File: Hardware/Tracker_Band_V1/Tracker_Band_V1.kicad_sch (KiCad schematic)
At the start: 5 parts, among them J1 USB_C_USB20, U1 ESP32-C3-MINI-1-N4, U2 BNO085

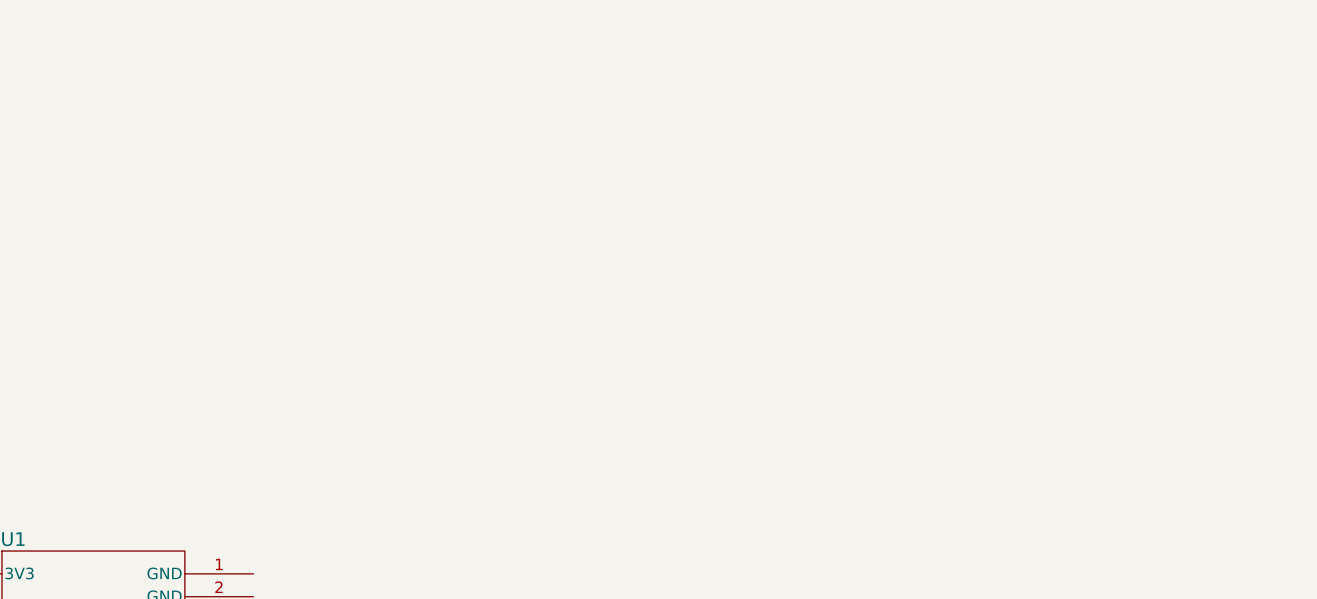
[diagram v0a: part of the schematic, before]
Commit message: added custom power sym/fp
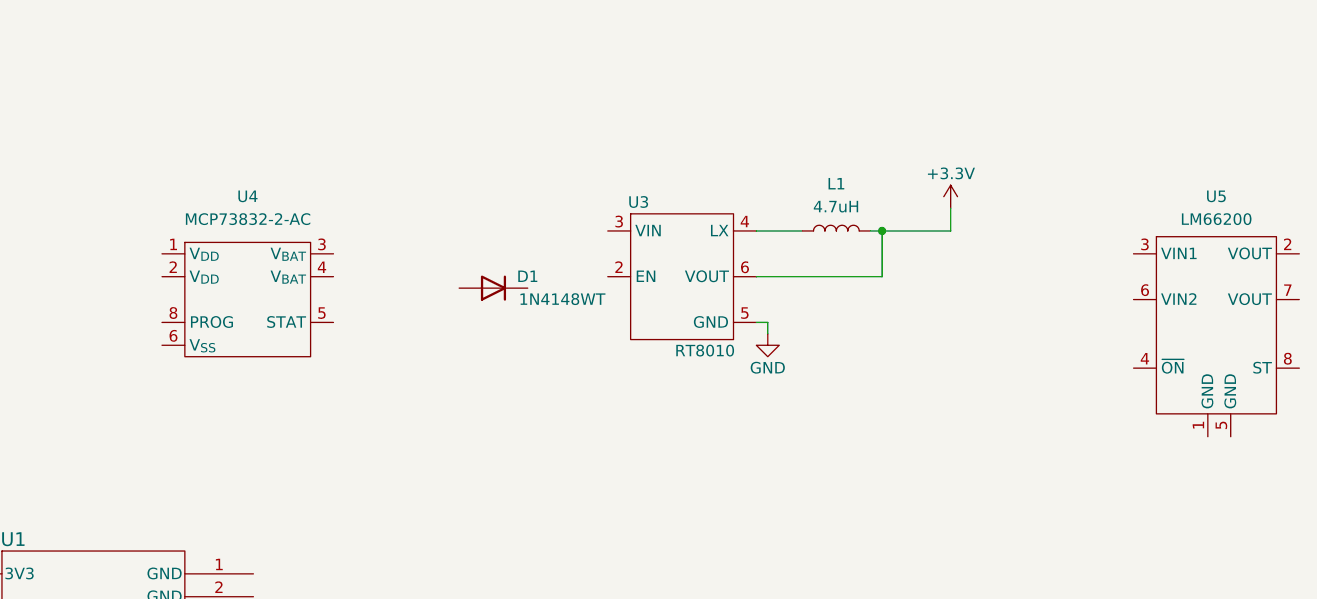
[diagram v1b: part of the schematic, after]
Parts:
- added D1: 1N4148WT, Diode_SMD:D_SOD-523, symbol Diode:1N4148WT
- added L1: 4.7uH, Inductor_SMD:L_Taiyo-Yuden_NR-30xx, symbol Device:L
- added U3: RT8010, Package_DFN_QFN:DFN-6-1EP_2x2mm_P0.65mm_EP1x1.6mm, symbol 00_tracker_sym:RT8010
- added U4: MCP73832-2-AC, Package_DFN_QFN:DFN-8-1EP_3x2mm_P0.5mm_EP1.7x1.4mm, symbol 00_tracker_sym:MCP73832-2-AC
- added U5: LM66200, 00_tracker_fp:SOT-5X3_DRL_TEX-L, symbol 00_tracker_sym:LM66200
- J1: footprint Connector_USB:USB_C_Receptacle_G-Switch_GT-USB-7010ASV -> 00_tracker_fp:USB_C_Receptacle_G-Switch_GT-USB-7010ASV_local3d
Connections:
- net +3.3V: now also L1.2, U3.6 (VOUT)
- net GND: now also U3.5 (GND)
- new net: L1.1, U3.4 (LX)
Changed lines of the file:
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@@
 (kicad_sch (version 20230121) (generator eeschema)
   (paper "A3")
+  (junction (at 278.13 64.77) (diameter 0) (color 0 0 0 0)
+  )
   (wire (pts (xy 125.73 114.3) (xy 125.73 115.57))
     (stroke (width 0) (type default))
   )
+  (wire (pts (xy 278.13 64.77) (xy 276.86 64.77))
+    (stroke (width 0) (type default))
+  )
+  (wire (pts (xy 264.16 69.85) (xy 278.13 69.85))
+    (stroke (width 0) (type default))
+  )
+  (wire (pts (xy 265.43 76.2) (xy 265.43 74.93))
+    (stroke (width 0) (type default))
+  )
+  (wire (pts (xy 278.13 69.85) (xy 278.13 64.77))
+    (stroke (width 0) (type default))
+  )
+  (wire (pts (xy 265.43 74.93) (xy 264.16 74.93))
+    (stroke (width 0) (type default))
+  )
   (wire (pts (xy 125.73 93.98) (xy 125.73 95.25))
     (stroke (width 0) (type default))
   )
+  (wire (pts (xy 285.75 62.23) (xy 285.75 64.77))
+    (stroke (width 0) (type default))
+  )
+  (wire (pts (xy 285.75 64.77) (xy 278.13 64.77))
+    (stroke (width 0) (type default))
+  )
   (wire (pts (xy 125.73 100.33) (xy 125.73 109.22))
+    (stroke (width 0) (type default))
+  )
+  (wire (pts (xy 264.16 64.77) (xy 269.24 64.77))
     (stroke (width 0) (type default))
   )
@@
     (effects (font (size 1.27 1.27)) (justify left bottom))
   )
+  (symbol (lib_id "Diode:1N4148WT") (at 234.95 71.12 180) (unit 1)
+    (in_bom yes) (on_board yes) (dnp no)
+    (property "Reference" "D1" (at 238.76 69.85 0)
+      (effects (font (size 1.27 1.27)))
+    )
+    (property "Value" "1N4148WT" (at 242.57 72.39 0)
+      (effects (font (size 1.27 1.27)))
+    )
+    (property "Footprint" "Diode_SMD:D_SOD-523" (at 234.95 66.675 0)
+      (effects (font (size 1.27 1.27)) hide)
+    )
+    (property "Datasheet" "https://www.diodes.com/assets/Datasheets/ds30396.pdf" (at 234.95 71.12 0)
+      (effects (font (size 1.27 1.27)) hide)
+    )
+    (property "Sim.Device" "D" (at 234.95 71.12 0)
+      (effects (font (size 1.27 1.27)) hide)
+    )
+    (property "Sim.Pins" "1=K 2=A" (at 234.95 71.12 0)
+      (effects (font (size 1.27 1.27)) hide)
+    )
+    (pin "1")
+    (pin "2")
+    (instances
+      (project "Tracker_Band_V1"
+        (path "/38c4babf-9cde-4e06-a603-1df616028c2e"
+          (reference "D1") (unit 1)
+        )
+      )
+    )
+  )
   (symbol (lib_id "00_tracker_sym:BNO085") (at 227.33 119.38 0) (unit 1)
     (in_bom yes) (on_board yes) (dnp no)
@@
       (effects (font (size 1.27 1.27)) (justify left) hide)
     )
-    (property "Datasheet" "" (at 250.19 124.46 0)
+    (property "Datasheet" "${KIPRJMOD}/datasheets/BNO080_085-Datasheet.pdf" (at 250.19 124.46 0)
       (effects (font (size 1.27 1.27)) hide)
     )
@@
     )
   )
+  (symbol (lib_id "power:+3.3V") (at 285.75 62.23 0) (unit 1)
+    (in_bom yes) (on_board yes) (dnp no)
+    (property "Reference" "#PWR03" (at 285.75 66.04 0)
+      (effects (font (size 1.27 1.27)) hide)
+    )
+    (property "Value" "+3.3V" (at 285.75 58.42 0)
+      (effects (font (size 1.27 1.27)))
+    )
+    (property "Footprint" "" (at 285.75 62.23 0)
+      (effects (font (size 1.27 1.27)) hide)
+    )
+    (property "Datasheet" "" (at 285.75 62.23 0)
+      (effects (font (size 1.27 1.27)) hide)
+    )
+    (pin "1")
+    (instances
+      (project "Tracker_Band_V1"
+        (path "/38c4babf-9cde-4e06-a603-1df616028c2e"
+          (reference "#PWR03") (unit 1)
+        )
+      )
+    )
+  )
+  (symbol (lib_id "Device:L") (at 273.05 64.77 90) (unit 1)
+    (in_bom yes) (on_board yes) (dnp no) (fields_autoplaced)
+    (property "Reference" "L1" (at 273.05 59.563 90)
+      (effects (font (size 1.27 1.27)))
+    )
+    (property "Value" "4.7uH" (at 273.05 62.103 90)
+      (effects (font (size 1.27 1.27)))
+    )
+    (property "Footprint" "Inductor_SMD:L_Taiyo-Yuden_NR-30xx" (at 273.05 64.77 0)
+      (effects (font (size 1.27 1.27)) hide)
+    )
+    (property "Datasheet" "~" (at 273.05 64.77 0)
+      (effects (font (size 1.27 1.27)) hide)
+    )
+    (pin "1")
+    (pin "2")
+    (instances
+      (project "Tracker_Band_V1"
+        (path "/38c4babf-9cde-4e06-a603-1df616028c2e"
+          (reference "L1") (unit 1)
+        )
+      )
+    )
+  )
   (symbol (lib_id "Connector:USB_C_Receptacle_USB2.0_16P") (at 132.08 143.51 0) (unit 1)
     (in_bom yes) (on_board yes) (dnp no)
@@
       (effects (font (size 1.27 1.27)))
     )
-    (property "Footprint" "Connector_USB:USB_C_Receptacle_G-Switch_GT-USB-7010ASV" (at 135.89 143.51 0)
+    (property "Footprint" "00_tracker_fp:USB_C_Receptacle_G-Switch_GT-USB-7010ASV_local3d" (at 135.89 143.51 0)
       (effects (font (size 1.27 1.27)) hide)
     )
@@
     )
   )
+  (symbol (lib_id "00_tracker_sym:MCP73832-2-AC") (at 198.12 67.31 0) (unit 1)
+    (in_bom yes) (on_board yes) (dnp no) (fields_autoplaced)
+    (property "Reference" "U4" (at 207.645 60.96 0)
+      (effects (font (size 1.27 1.27)))
+    )
+    (property "Value" "MCP73832-2-AC" (at 207.645 63.5 0)
+      (effects (font (size 1.27 1.27)))
+    )
+    (property "Footprint" "Package_DFN_QFN:DFN-8-1EP_3x2mm_P0.5mm_EP1.7x1.4mm" (at 193.675 86.36 0)
+      (effects (font (size 1.27 1.27) italic) (justify left) hide)
+    )
+    (property "Datasheet" "${KIPRJMOD}/datasheets/MCP73831-Family-Data-Sheet-DS20001984H.pdf" (at 231.14 83.82 0)
+      (effects (font (size 1.27 1.27)) hide)
+    )
+    (pin "4")
+    (pin "8")
+    (pin "5")
+    (pin "1")
+    (pin "7")
+    (pin "6")
+    (pin "2")
+    (pin "3")
+    (instances
+      (project "Tracker_Band_V1"
+        (path "/38c4babf-9cde-4e06-a603-1df616028c2e"
+          (reference "U4") (unit 1)
+        )
+      )
+    )
+  )
   (symbol (lib_id "power:GND") (at 125.73 115.57 0) (unit 1)
     (in_bom yes) (on_board yes) (dnp no)
@@
         (path "/38c4babf-9cde-4e06-a603-1df616028c2e"
           (reference "#PWR02") (unit 1)
+        )
+      )
+    )
+  )
+  (symbol (lib_id "00_tracker_sym:RT8010") (at 247.65 64.77 0) (unit 1)
+    (in_bom yes) (on_board yes) (dnp no)
+    (property "Reference" "U3" (at 251.079 61.595 0)
+      (effects (font (size 1.27 1.27)))
+    )
+    (property "Value" "RT8010" (at 258.445 78.105 0)
+      (effects (font (size 1.27 1.27)))
+    )
+    (property "Footprint" "Package_DFN_QFN:DFN-6-1EP_2x2mm_P0.65mm_EP1x1.6mm" (at 277.495 59.055 0)
+      (effects (font (size 1.27 1.27)) hide)
+    )
+    (property "Datasheet" "${KIPRJMOD}/datasheets/DS8010A-12.pdf" (at 268.605 57.15 0)
+      (effects (font (size 1.27 1.27)) hide)
+    )
+    (pin "1")
+    (pin "6")
+    (pin "5")
+    (pin "2")
+    (pin "3")
+    (pin "4")
+    (instances
+      (project "Tracker_Band_V1"
+        (path "/38c4babf-9cde-4e06-a603-1df616028c2e"
+          (reference "U3") (unit 1)
+        )
+      )
+    )
+  )
+  (symbol (lib_id "power:GND") (at 265.43 76.2 0) (unit 1)
+    (in_bom yes) (on_board yes) (dnp no)
+    (property "Reference" "#PWR04" (at 265.43 82.55 0)
+      (effects (font (size 1.27 1.27)) hide)
+    )
+    (property "Value" "GND" (at 265.43 80.01 0)
+      (effects (font (size 1.27 1.27)))
+    )
+    (property "Footprint" "" (at 265.43 76.2 0)
+      (effects (font (size 1.27 1.27)) hide)
+    )
+    (property "Datasheet" "" (at 265.43 76.2 0)
+      (effects (font (size 1.27 1.27)) hide)
+    )
+    (pin "1")
+    (instances
+      (project "Tracker_Band_V1"
+        (path "/38c4babf-9cde-4e06-a603-1df616028c2e"
+          (reference "#PWR04") (unit 1)
         )
       )
@@
       (effects (font (size 1.27 1.27) italic) (justify left) hide)
     )
-    (property "Datasheet" "ESP32-C3-MINI-1-N4" (at 179.07 87.63 0)
+    (property "Datasheet" "${KIPRJMOD}/datasheets/esp32-c3-mini-1_datasheet_en.pdf" (at 179.07 87.63 0)
       (effects (font (size 1.27 1.27) italic) (justify left) hide)
     )
@@
         )
       )
+    )
+  )
+  (symbol (lib_id "00_tracker_sym:LM66200") (at 306.07 67.31 0) (unit 1)
+    (in_bom yes) (on_board yes) (dnp no) (fields_autoplaced)
+    (property "Reference" "U5" (at 315.2775 60.96 0)
+      (effects (font (size 1.27 1.27)))
+    )
+    (property "Value" "LM66200" (at 315.2775 63.5 0)
+      (effects (font (size 1.27 1.27)))
+    )
+    (property "Footprint" "00_tracker_fp:SOT-5X3_DRL_TEX-L" (at 319.405 56.515 0)
+      (effects (font (size 1.27 1.27)) hide)
+    )
+    (property "Datasheet" "${KIPRJMOD}/datasheets/lm66200.pdf" (at 321.31 59.69 0)
+      (effects (font (size 1.27 1.27)) hide)
+    )
+    (pin "3")
+    (pin "1")
+    (pin "2")
+    (pin "4")
+    (pin "5")
+    (pin "7")
+    (pin "6")
+    (pin "8")
+    (instances
+      (project "Tracker_Band_V1"
+        (path "/38c4babf-9cde-4e06-a603-1df616028c2e"
+          (reference "U5") (unit 1)
+        )
+      )

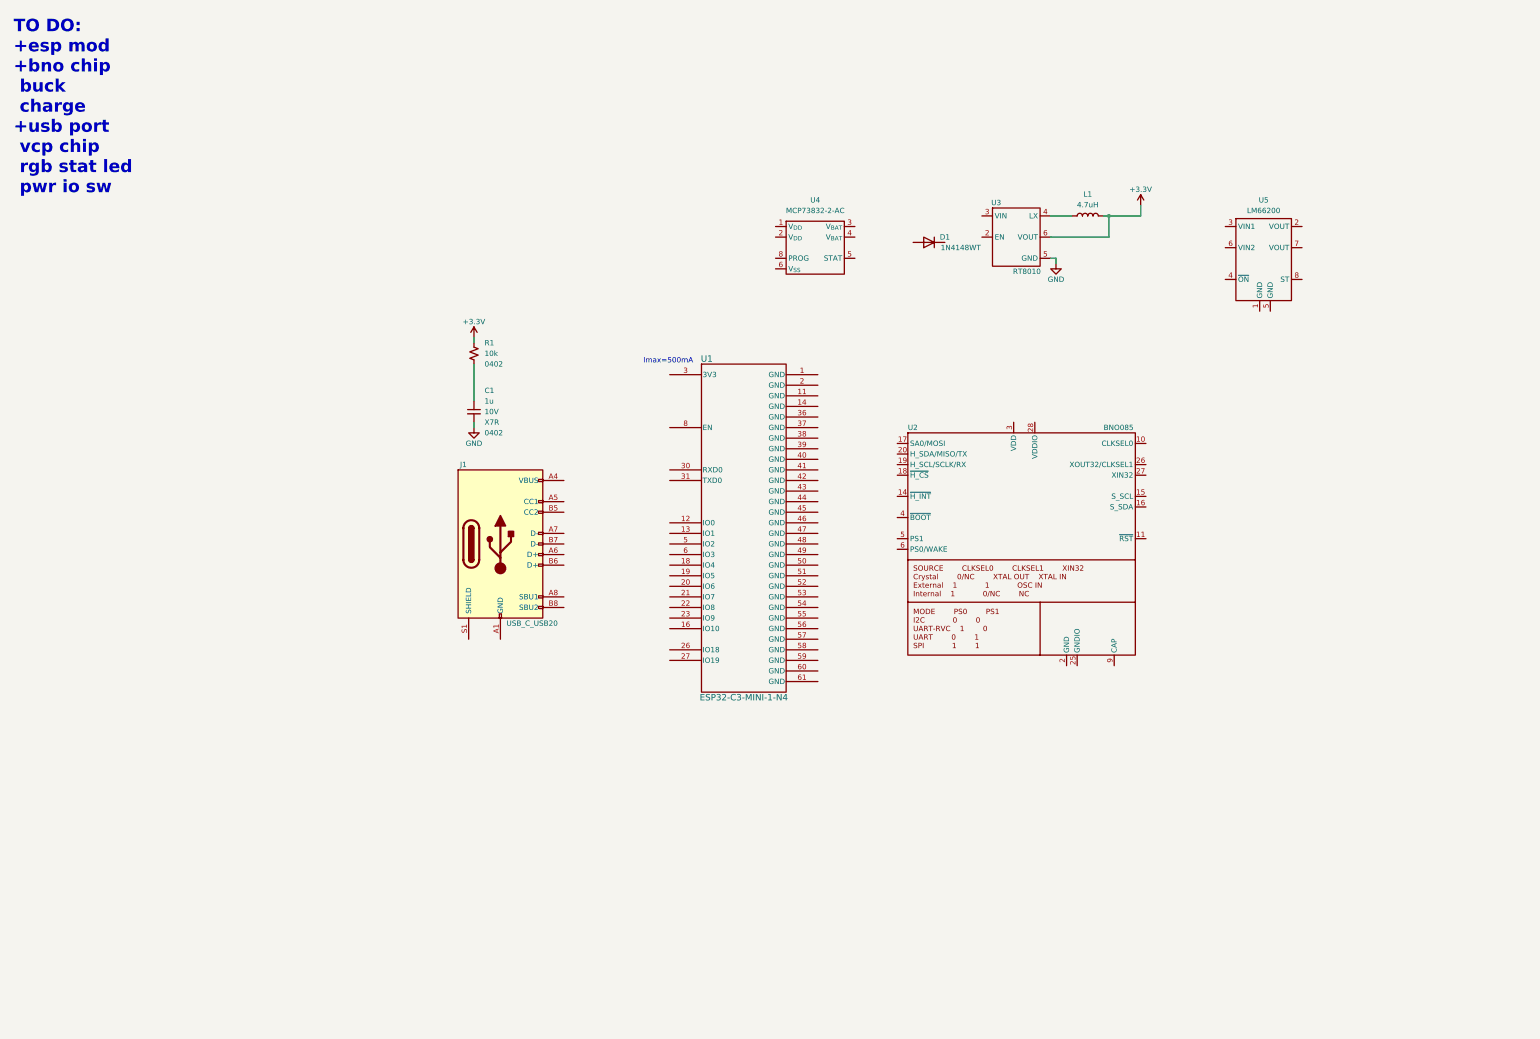
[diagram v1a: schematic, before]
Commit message: Updated schematic wiring
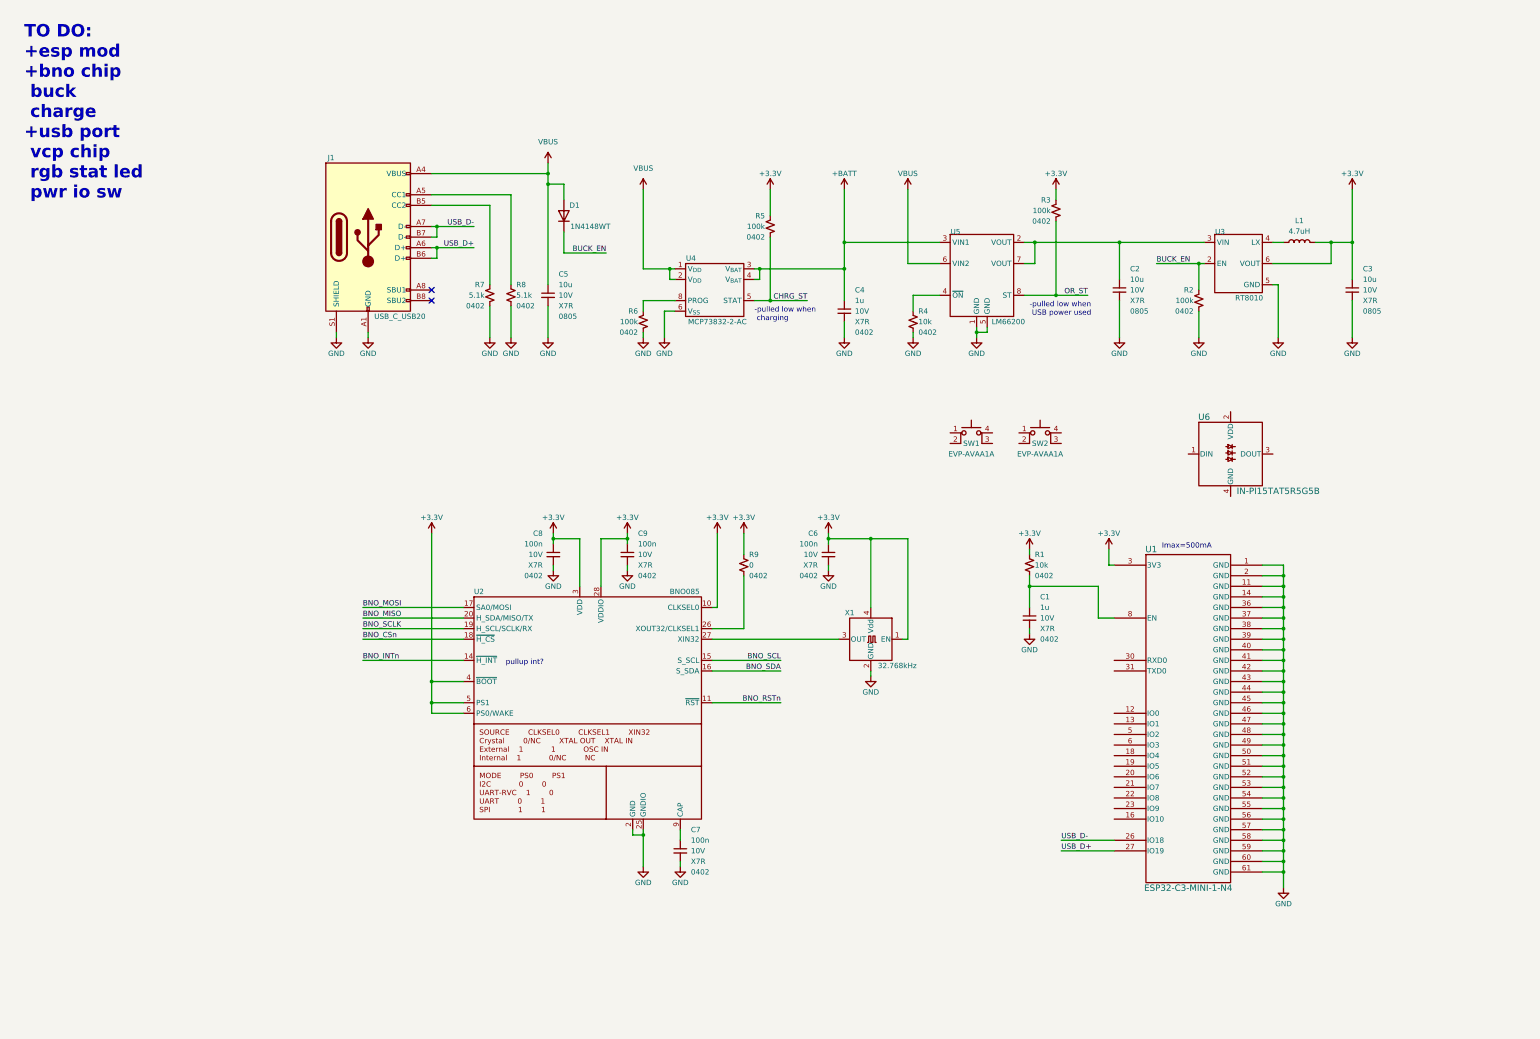
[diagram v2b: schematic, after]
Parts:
- added C2, C3: 10u, Capacitor_SMD:C_0805_2012Metric, symbol Device:C_Small
- added C4: 1u, Capacitor_SMD:C_0402_1005Metric, symbol Device:C_Small
- added C5: 10u, Capacitor_SMD:C_0402_1005Metric, symbol Device:C_Small
- added C6, C7, C8, C9: 100n, Capacitor_SMD:C_0402_1005Metric, symbol Device:C_Small
- added R2, R3, R5, R6: 100k, Resistor_SMD:R_0402_1005Metric, symbol Device:R_Small_US
- added R4: 10k, Resistor_SMD:R_0402_1005Metric, symbol Device:R_Small_US
- added R7, R8: 5.1k, Resistor_SMD:R_0402_1005Metric, symbol Device:R_Small_US
- added R9: 0, Resistor_SMD:R_0402_1005Metric, symbol Device:R_Small_US
- added SW1, SW2: EVP-AVAA1A, 00_tracker_fp:EVP-AVAA1A_PAN, symbol Switch:SW_MEC_5E
- added U6: IN-PI15TAT5R5G5B, 00_tracker_fp:IN-PI15_INL, symbol 00_tracker_sym:IN-PI15TAT5R5G5B
- added X1: 32.768kHz, 00_tracker_fp:OSC_ECS-1618-300-BN-TR, symbol 00_tracker_sym:ECS-327MVATX
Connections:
- net +3.3V: now also U1.3 (3V3), U2.10 (CLKSEL0), U2.28 (VDDIO), U2.3 (VDD), U2.4 (~{BOOT}), U2.5 (PS1), U2.6 (PS0/WAKE), C3.1, C6.1, C8.1, C9.1, R3.1, R5.1, R9.1, X1.1 (EN), X1.4 (Vdd)
- net GND: now also J1.A1 (GND), J1.A12 (GND), J1.B1 (GND), J1.B12 (GND), J1.S1 (SHIELD), U1.1 (GND), U1.11 (GND), U1.14 (GND), U1.2 (GND), U1.36 (GND), U1.37 (GND), U1.38 (GND), U1.39 (GND), U1.40 (GND), U1.41 (GND), U1.42 (GND), U1.43 (GND), U1.44 (GND), U1.45 (GND), U1.46 (GND), U1.47 (GND), U1.48 (GND), U1.49 (GND), U1.50 (GND), U1.51 (GND), U1.52 (GND), U1.53 (GND), U1.54 (GND), U1.55 (GND), U1.56 (GND), U1.57 (GND), U1.58 (GND), U1.59 (GND), U1.60 (GND), U1.61 (GND), U2.2 (GND), U2.25 (GNDIO), U4.6 (V_{SS}), U5.1 (GND), U5.5 (GND), C2.2, C3.2, C4.2, C5.2, C6.2, C7.2, C8.2, C9.2, R2.2, R4.2, R6.2, R7.2, R8.2, X1.2 (GND)
- net BUCK_EN: now reaches D1.1 (K)
- net BUCK_EN: now also U3.2 (EN), R2.1
- net VBUS: now reaches D1.2 (A)
- net VBUS: now also J1.A4 (VBUS), J1.A9 (VBUS), J1.B4 (VBUS), J1.B9 (VBUS), U4.1 (V_{DD}), U4.2 (V_{DD}), U5.6 (VIN2), C5.1
- net BNO_RSTn: now reaches U2.11 (~{RST})
- net BNO_INTn: now reaches U2.14 (~{H_INT})
- net BNO_SCL: now reaches U2.15 (S_SCL)
- net BNO_SDA: now reaches U2.16 (S_SDA)
- net BNO_MOSI: now reaches U2.17 (SA0/MOSI)
- net BNO_CSn: now reaches U2.18 (~{H_CS})
- net BNO_SCLK: now reaches U2.19 (H_SCL/SCLK/RX)
- net BNO_MISO: now reaches U2.20 (H_SDA/MISO/TX)
- net at U2.26 (XOUT32/CLKSEL1): now also R9.2
- net at U2.27 (XIN32): now also X1.3 (OUT)
- net at U2.9 (CAP): now also C7.1
- net at C1.1, R1.2: now also U1.8 (EN)
- net at J1.A5 (CC1): now also R8.1
- net USB_D+: now reaches J1.A6 (D+)
- net USB_D+: now also J1.B6 (D+), U1.27 (IO19)
- net USB_D-: now reaches J1.A7 (D-)
- net USB_D-: now also J1.B7 (D-), U1.26 (IO18)
- net at J1.B5 (CC2): now also R7.1
- net +BATT: now reaches U4.3 (V_{BAT})
- net +BATT: now also U4.4 (V_{BAT}), U5.3 (VIN1), C4.1
- net CHRG_ST: now reaches U4.5 (STAT)
- net CHRG_ST: now also R5.2
- net at U4.8 (PROG): now also R6.1
- net at U3.3 (VIN): now also U5.2 (VOUT), U5.7 (VOUT), C2.1
- net at U5.4 (~{ON}): now also R4.1
- net OR_ST: now reaches U5.8 (ST)
- net OR_ST: now also R3.2
- no-connect marks 0 -> 2
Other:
- note added: "-pulled low when USB power used"
- note added: "-pulled low when charging"
- note added: "pullup int?"
- moved on the sheet: C1, D1, J1, L1, R1, U1, U2, U3, U4, U5
